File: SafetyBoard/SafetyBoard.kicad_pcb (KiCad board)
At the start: 4 copper layers, 154 x 93 mm, 170 parts, among them J1 Estop, J10 TSSI, J11 ACCU, J12 BBC, J13 614004135023, J14 footwell, J15 RTD B, J16 Brakelight, J17 SHOCK/WHEEL SNSR, J18 39306207, J19 AMP, J2 TS ON SW, J3 SDC OUT, J4 ACCU, J5 12v EXP, J6 PWR IN, J7 24v EXP, J8 5v EXP, J9 Current Sensor, K1 G6B-2214P-US DC12, K2 G6B-2214P-US DC12, K3 G6B-2214P-US DC12, Q1 IRLIZ44N NMOS, Q2 IRLIZ44N NMOS, Q3 IRLIZ44N NMOS, Q4 IRLIZ44N NMOS, Q5 PMOS IRF9540, Q6 PMOS IRF9540, Q7 PMOS IRF9540, SW1 SW_Push, SW2 SW_Push, SW3 SW_Push, U1 40106 Inverter, U2 4081 AND Gate, U3 LT1084-5.0, U4 LM393, U5 LM393, U6 CD4071BE OR Gate, U7 LM393, U8 LM555xN, U9 OKX-T/5-D12N-C

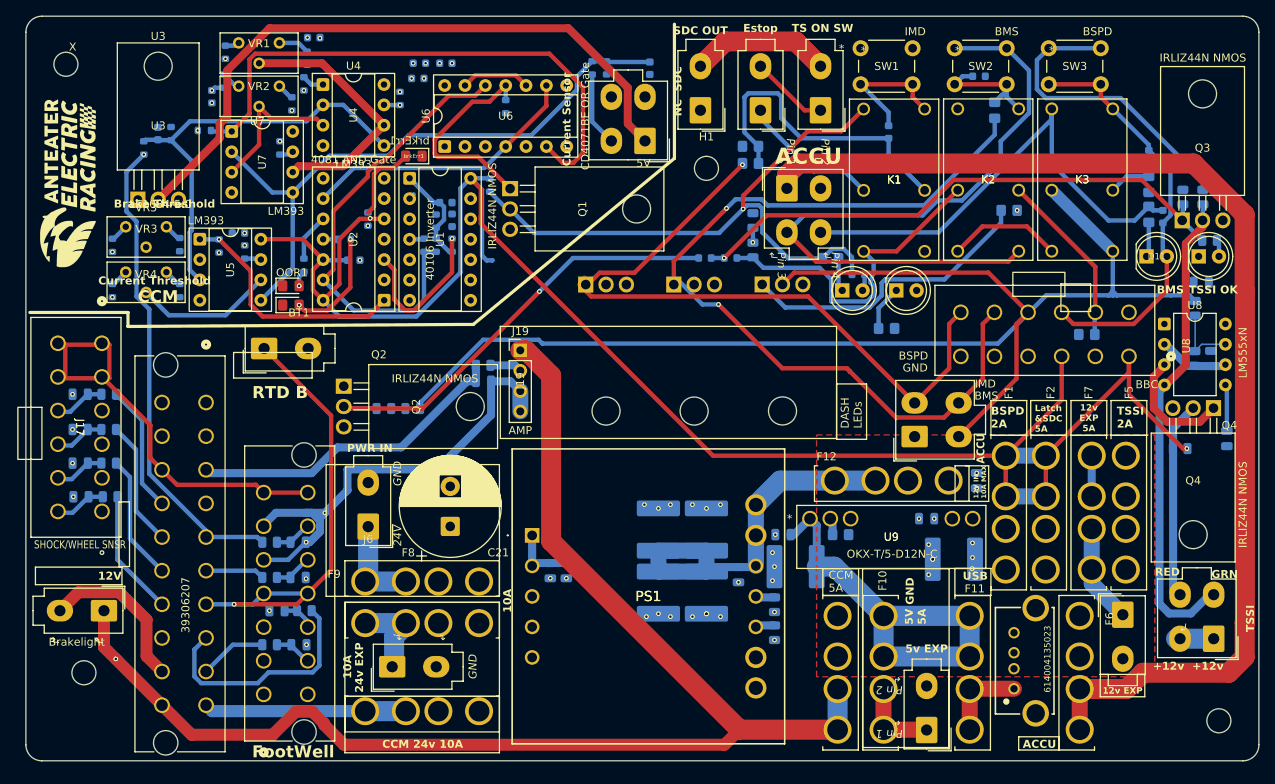
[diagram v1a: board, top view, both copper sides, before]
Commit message: Increased trace width
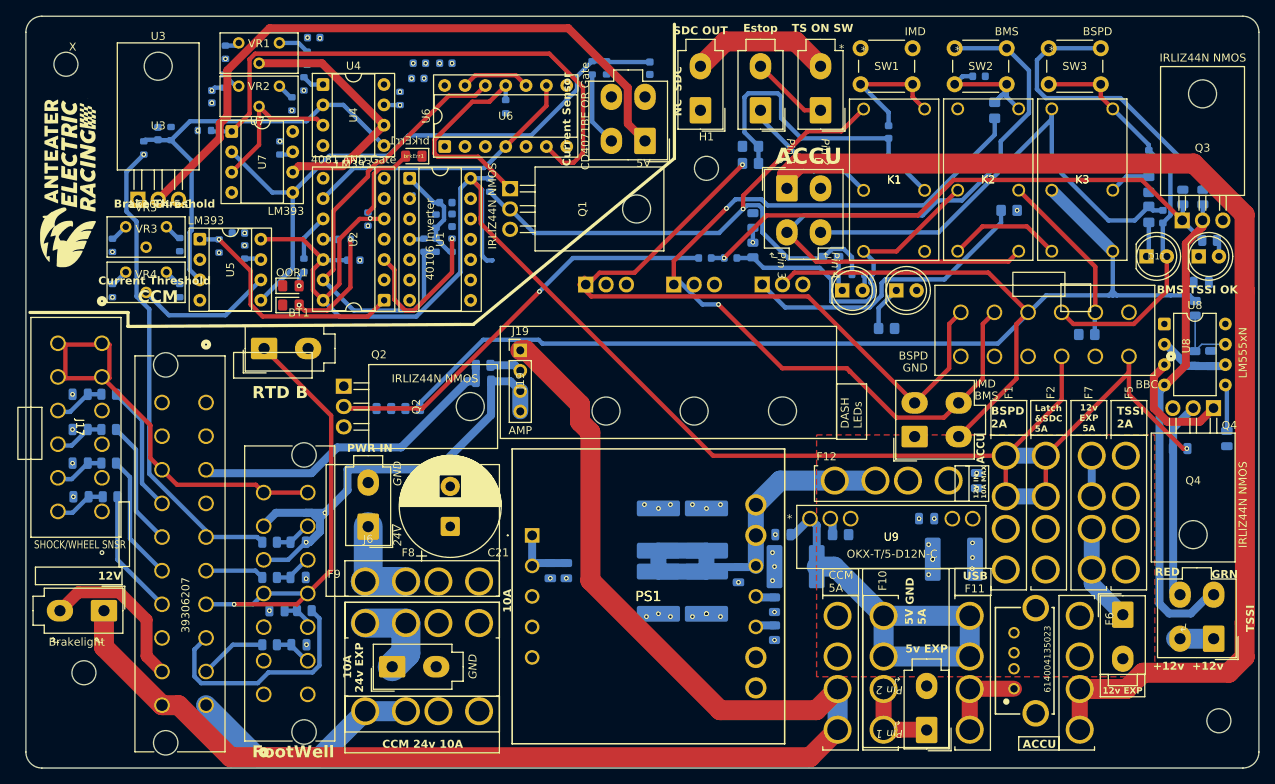
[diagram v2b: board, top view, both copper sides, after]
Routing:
- net /CCM Helper/12V: track 168.7 -> 179.8 mm, vias 1 -> 0
- net /CCM Helper/24V: track 25.3 -> 30.0 mm
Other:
- board size 154 x 93 mm -> 154 x 93.9 mm
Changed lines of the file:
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@@
 			)
 		)
-		(fp_text user "↲"
-			(at 3.048 1.27 90)
-			(unlocked yes)
-			(layer "F.SilkS")
-			(effects
-				(font
-					(size 1 1)
-					(thickness 0.1)
-					(italic yes)
-				)
-				(justify left bottom)
-			)
-		)
-		(fp_text user "↲"
-			(at 3.048 6.731 90)
-			(unlocked yes)
-			(layer "F.SilkS")
-			(effects
-				(font
-					(size 1 1)
-					(thickness 0.1)
-					(italic yes)
-				)
-				(justify left bottom)
-			)
-		)
 		(fp_text user "${REFERENCE}"
 			(at 0 -1.55 90)
@@
 	)
 	(gr_arc
-		(start 223 161)
-		(mid 222.414214 162.414214)
-		(end 221 163)
+		(start 223 161.9)
+		(mid 222.414214 163.314214)
+		(end 221 163.9)
 		(stroke
 			(width 0.05)
@@
 	(gr_line
 		(start 223 72)
-		(end 223 161)
+		(end 223 161.9)
 		(stroke
 			(width 0.05)
@@
 	)
 	(gr_arc
-		(start 71 163)
-		(mid 69.585786 162.414214)
-		(end 69 161)
+		(start 71 163.9)
+		(mid 69.585786 163.314214)
+		(end 69 161.9)
 		(stroke
 			(width 0.05)
@@
 	)
 	(gr_line
-		(start 221 163)
-		(end 71 163)
+		(start 221 163.9)
+		(end 71 163.9)
 		(stroke
 			(width 0.05)
@@
 	)
 	(gr_line
-		(start 69 161)
+		(start 69 161.9)
 		(end 69 72)
 		(stroke
@@
 		)
 	)
+	(dimension
+		(type orthogonal)
+		(layer "Dwgs.User")
+		(pts
+			(xy 71 70) (xy 71 163.9)
+		)
+		(height -10.9)
+		(orientation 1)
+		(format
+			(prefix "")
+			(suffix "")
+			(units 3)
+			(units_format 0)
+			(precision 4)
+			(suppress_zeroes yes)
+		)
+		(style
+			(thickness 0.1)
+			(arrow_length 1.27)
+			(text_position_mode 2)
+			(arrow_direction outward)
+			(extension_height 0.58642)
+			(extension_offset 0.5)
+			(keep_text_aligned yes)
+		)
+		(gr_text "93.9"
+			(at 58.6 117.1 90)
+			(layer "Dwgs.User")
+			(effects
+				(font
+					(size 1 1)
+					(thickness 0.15)
+				)
+			)
+		)
+	)
+	(dimension
+		(type orthogonal)
+		(layer "Dwgs.User")
+		(pts
+			(xy 223 71) (xy 69 71)
+		)
+		(height -3)
+		(orientation 0)
+		(format
+			(prefix "")
+			(suffix "")
+			(units 3)
+			(units_format 0)
+			(precision 4)
+			(suppress_zeroes yes)
+		)
+		(style
+			(thickness 0.1)
+			(arrow_length 1.27)
+			(text_position_mode 0)
+			(arrow_direction outward)
+			(extension_height 0.58642)
+			(extension_offset 0.5)
+			(keep_text_aligned yes)
+		)
+		(gr_text "154"
+			(at 146 66.85 0)
+			(layer "Dwgs.User")
+			(effects
+				(font
+					(size 1 1)
+					(thickness 0.15)
+				)
+			)
+		)
+	)
 	(via
 		(at 102.2245 81.7745)
@@
 	)
 	(segment
-		(start 106.265003 158.354112)
-		(end 106.265003 158.515003)
-		(width 1.5)
-		(layer "F.Cu")
-		(net 73)
-	)
-	(segment
-		(start 104.785892 156.875001)
-		(end 106.265003 158.354112)
-		(width 1.5)
+		(start 170.38 154.03)
+		(end 167.7365 156.6735)
+		(width 2.5)
 		(layer "F.Cu")
 		(net 73)
 	)
 	(segment
-		(start 102.694114 156.875001)
-		(end 104.785892 156.875001)
-		(width 1.5)
+		(start 86 156.049997)
+		(end 88.065015 156.049997)
+		(width 2.5)
 		(layer "F.Cu")
 		(net 73)
 	)
 	(segment
-		(start 99.819115 159.75)
-		(end 102.694114 156.875001)
-		(width 1.5)
+		(start 131.464106 111.7375)
+		(end 130.75 111.7375)
+		(width 2.5)
 		(layer "F.Cu")
 		(net 73)
 	)
 	(segment
-		(start 89.700003 159.75)
-		(end 99.819115 159.75)
-		(width 1.5)
+		(start 139.5 121.952808)
+		(end 138.209 120.661808)
+		(width 2.5)
 		(layer "F.Cu")
 		(net 73)
 	)
 	(segment
-		(start 86 156.049997)
-		(end 89.700003 159.75)
-		(width 1.5)
+		(start 138.209 118.482394)
+		(end 131.464106 111.7375)
+		(width 2.5)
 		(layer "F.Cu")
 		(net 73)
 	)
 	(segment
-		(start 170.38 159.11)
-		(end 158.133712 159.11)
+		(start 138.209 120.661808)
+		(end 138.209 118.482394)
 		(width 2.5)
 		(layer "F.Cu")
@@
 	)
 	(segment
-		(start 156.243712 161)
-		(end 158.133712 159.11)
-		(width 1.5)
+		(start 139.5 140.476288)
+		(end 139.5 121.952808)
+		(width 2.5)
 		(layer "F.Cu")
 		(net 73)
@@
 	(segment
 		(start 78.75 144.25)
-		(end 78.75 148.799998)
-		(width 1.5)
-		(layer "F.Cu")
-		(net 73)
-	)
-	(segment
-		(start 108.75 161)
-		(end 156.243712 161)
-		(width 1.5)
-		(layer "F.Cu")
-		(net 73)
-	)
-	(segment
-		(start 134.596 135.572288)
-		(end 134.596 114.869394)
+		(end 78.75 148.799997)
 		(width 2.5)
 		(layer "F.Cu")
@@
 	)
 	(segment
-		(start 134.596 114.869394)
-		(end 131.464106 111.7375)
+		(start 88.065015 156.049997)
+		(end 94.564018 162.549)
 		(width 2.5)
 		(layer "F.Cu")
@@
 	)
 	(segment
-		(start 106.265003 158.515003)
-		(end 108.75 161)
-		(width 1.5)
+		(start 166.941 162.549)
+		(end 170.38 159.11)
+		(width 2.5)
 		(layer "F.Cu")
 		(net 73)
 	)
 	(segment
-		(start 131.464106 111.7375)
-		(end 130.75 111.7375)
+		(start 155.697212 156.6735)
+		(end 139.5 140.476288)
 		(width 2.5)
 		(layer "F.Cu")
@@
 	)
 	(segment
-		(start 158.133712 159.11)
-		(end 134.596 135.572288)
+		(start 78.75 148.799997)
+		(end 86 156.049997)
 		(width 2.5)
 		(layer "F.Cu")
@@
 	)
 	(segment
-		(start 78.75 148.799998)
-		(end 80.225001 150.274999)
-		(width 1.5)
+		(start 167.7365 156.6735)
+		(end 155.697212 156.6735)
+		(width 2.5)
 		(layer "F.Cu")
 		(net 73)
 	)
 	(segment
-		(start 80.225001 150.274999)
-		(end 86 156.049997)
-		(width 1.5)
+		(start 94.564018 162.549)
+		(end 166.941 162.549)
+		(width 2.5)
 		(layer "F.Cu")
 		(net 73)
 	)
-	(via
-		(at 80.225001 150.274999)
-		(size 0.6)
-		(drill 0.3)
-		(layers "F.Cu" "B.Cu")
-		(net 73)
-	)
 	(segment
 		(start 170.38 159.11)
@@
 	)
 	(segment
-		(start 116.46 156.8)
-		(end 111.38 156.8)
+		(start 97.999002 162.549)
+		(end 91.499999 156.049997)
 		(width 2.5)
 		(layer "B.Cu")
@@
 	)
 	(segment
-		(start 91.499999 156.049997)
-		(end 92.250002 156.8)
-		(width 1.5)
+		(start 105.631 162.549)
+		(end 97.999002 162.549)
+		(width 2.5)
 		(layer "B.Cu")
 		(net 91)
 	)
 	(segment
-		(start 92.250002 156.8)
-		(end 111.38 156.8)
-		(width 1.5)
+		(start 111.38 156.8)
+		(end 105.631 162.549)
+		(width 2.5)
+		(layer "B.Cu")
+		(net 91)
+	)
+	(segment
+		(start 111.38 156.8)
+		(end 116.46 156.8)
+		(width 2.5)
 		(layer "B.Cu")
 		(net 91)
@@
 	)
 	(segment
-		(start 111.75 133.75)
-		(end 111.75 140.23)
-		(width 2.5)
+		(start 111.75 140.23)
+		(end 111.38 140.6)
+		(width 3.618)
 		(layer "B.Cu")
 		(net 101)
 	)
 	(segment
-		(start 111.75 140.23)
-		(end 111.38 140.6)
-		(width 2.5)
+		(start 111.75 133.75)
+		(end 111.75 140.23)
+		(width 3.618)
 		(layer "B.Cu")
 		(net 101)
@@
 		(start 116.46 140.6)
 		(end 111.38 140.6)
-		(width 2.5)
+		(width 3.618)
 		(layer "B.Cu")
 		(net 101)
@@
 	)
 	(segment
-		(start 116.46 146.04)
-		(end 116.46 145.8)
-		(width 2.5)
-		(layer "B.Cu")
-		(net 109)
-	)
-	(segment
-		(start 114.99 151.01)
-		(end 114.99 147.51)
-		(width 2.5)
-		(layer "B.Cu")
-		(net 109)
-	)
-	(segment
-		(start 114.75 151.25)
-		(end 114.99 151.01)
-		(width 2.5)
+		(start 116.46 145.8)
+		(end 116.46 149.54)
+		(width 3.618)
 		(layer "B.Cu")
 		(net 109)
 	)
 	(segment
-		(start 114.99 147.51)
-		(end 116.46 146.04)
-		(width 2.5)
+		(start 111.38 145.8)
+		(end 116.46 145.8)
+		(width 3.618)
 		(layer "B.Cu")
 		(net 109)
 	)
 	(segment
-		(start 116.46 145.8)
-		(end 111.38 145.8)
-		(width 2.5)
+		(start 116.46 149.54)
+		(end 114.75 151.25)
+		(width 3.618)
 		(layer "B.Cu")
 		(net 109)
@@
 		(min_thickness 0.25)
 		(filled_areas_thickness no)
-		(fill yes
+		(fill
 			(thermal_gap 0.5)
 			(thermal_bridge_width 0.5)
@@
 		(polygon
 			(pts
-				(xy 69 108.945768) (xy 93.386191 108.916933) (xy 93.3196 119.126) (xy 105.664 119.0752) (xy 106.1212 163)
-				(xy 69 163)
+				(xy 69 108.945768) (xy 93.386191 108.916933) (xy 93.3196 119.126) (xy 105.664 119.0752) (xy 106.128194 163.671996)
+				(xy 69 163.671996)
 			)
 		)
@@
 		(min_thickness 0.25)
 		(filled_areas_thickness no)
-		(fill yes
+		(fill
 			(thermal_gap 0.5)
 			(thermal_bridge_width 0.5)
@@
 		(polygon
 			(pts
-				(xy 223 71) (xy 69 71) (xy 69 163) (xy 223 163)
+				(xy 223 71) (xy 69 71) (xy 69 163.9) (xy 223 163.9)
 			)
 		)
@@
 		(min_thickness 0.25)
 		(filled_areas_thickness no)
-		(fill yes
+		(fill
 			(thermal_gap 0.5)
 			(thermal_bridge_width 0.5)
@@
 		(polygon
 			(pts
-				(xy 108.379175 126.743583) (xy 143.4084 126.6952) (xy 144.715885 163) (xy 108.75 163)
+				(xy 108.379175 126.743583) (xy 143.4084 126.6952) (xy 144.741095 163.7) (xy 108.757159 163.7)
 			)
 		)

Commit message: Minor updates
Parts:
- J4: value ACCU -> HVB
- moved R54 0.07 mm to (79.3, 121.5)
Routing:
- net +12V: track 408.6 -> 297.8 mm, vias 17 -> 16
- net /TSSI/GLV: track 4.20 -> 107.4 mm
- net Net-(J5-Pin_1): track 17.4 -> 10.6 mm
- net /12V: track 0.00 -> 4.24 mm
- net /LATCH/BSPDfault_LED: track 61.7 -> 58.4 mm
- net /LATCH/IMDfault_LED: track 56.6 -> 54.5 mm
- net /CCM Helper/CCMGND: track 60.2 -> 59.0 mm
- net Net-(Q4-G): track 14.9 -> 15.5 mm
- net Net-(brkErr1-A): vias 0 -> 1
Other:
- board text added: "HVB"
- board text removed: "ACCU"

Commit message: real final
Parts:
- removed BT1, OOR1: APTD2012LSYCK, LED_SMD:LED_0805_2012Metric_Pad1.15x1.40mm_HandSolder
- added BothThreshold1: APTD2012LSYCK, LED_SMD:LED_0805_2012Metric_Pad1.15x1.40mm_HandSolder, F.Cu at (102.3, 106.1)
- added OutOfRange1: APTD2012LSYCK, LED_SMD:LED_0805_2012Metric_Pad1.15x1.40mm_HandSolder, F.Cu at (102.2, 103.7)
- J1, J15, J16, J2, J3, J5, J6, J7, J8: footprint footprints:Molex_Mini-Fit_Jr_5566-02A_2x01_P4.20mm_Vertical -> 0footprints:Molex_Mini-Fit_Jr_5566-02A_2x01_P4.20mm_Vertical
- J10, J11, J9: footprint footprints:Molex_Mini-Fit_Jr_5566-04A_2x02_P4.20mm_Vertical -> 0footprints:Molex_Mini-Fit_Jr_5566-04A_2x02_P4.20mm_Vertical
- J4: value HVB -> ACCU; footprint footprints:Molex_Mini-Fit_Jr_5566-04A_2x02_P4.20mm_Vertical -> 0footprints:Molex_Mini-Fit_Jr_5566-04A_2x02_P4.20mm_Vertical
- brkErr1: moved to B.Cu
- moved H1 55.9 mm to (207.9, 74.1)
- moved R38 10.7 mm to (172.0, 110.7)
- moved D7 6.15 mm to (172.9, 108.4)
- moved C14 0.30 mm to (103.0, 148.2)
- moved C19 0.30 mm to (103.0, 139.8)
- moved J14 0.30 mm to (98.7, 154.4)
- moved SW3 0.25 mm to (196.5, 74.0)
- moved R55 0.22 mm to (79.3, 125.6)
- moved C15 0.21 mm to (100.3, 144.0)
- moved R46 0.21 mm to (103.7, 144.0)
- moved C18 0.21 mm to (103.0, 135.5)
- moved R45 0.21 mm to (99.4, 148.3)
- moved R47 0.21 mm to (99.4, 135.5)
- moved R48 0.21 mm to (99.4, 139.9)
- moved R56 0.12 mm to (79.5, 129.9)
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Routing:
- net +12V: track 297.8 -> 238.0 mm, vias 16 -> 30
- net /LATCH/BMSfault_LED: track 52.4 -> 88.9 mm, vias 0 -> 7
- net GND: track 0.00 -> 17.9 mm, vias 34 -> 59
- net /LATCH/BSPDfault_LED: track 58.4 -> 74.9 mm
- net Net-(J5-Pin_1): track 10.6 -> 25.3 mm
- net /LATCH/IMDfault_LED: track 54.5 -> 67.3 mm, vias 1 -> 6
- net /LATCH/bms_imd_latch_only: track 42.5 -> 31.1 mm, vias 0 -> 1
- net Net-(J6-Pin_1): track 12.7 -> 21.5 mm
- net /BSPD/PEDAL_OPEN: track 31.8 -> 39.3 mm, vias 0 -> 3
- net Net-(J7-Pin_1): track 11.2 -> 18.1 mm
- net /BSPD/BSPD_FAULT: track 77.6 -> 83.9 mm
- net /CCM Helper/CCM fdbk: track 81.9 -> 87.4 mm, vias 1 -> 2
- net /12V: track 4.24 -> 0.00 mm
- net Net-(D2-K): track 70.5 -> 74.5 mm
- net Net-(D6-K): track 4.80 -> 8.55 mm, vias 0 -> 1
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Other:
- board text added: "OC"
- board text added: "SC"
- board text added: "Safety Board By: Gabriel Schoene, Lucas Li, Avadi Seneviratne"
- board text added: "cursns"
- board text removed: "CCM"
- board text removed: "Safety Board By: Gabriel Schoene"

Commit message: double checking its all pushed
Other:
- board text added: "there better be a dummy plug in SDC con"
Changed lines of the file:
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@@
 		)
 		(property "Value" "Brakelight"
-			(at 0 9.95 270)
+			(at 9.45 7.35 270)
 			(layer "F.SilkS")
 			(effects
@@
 			(layer "F.Fab")
 		)
-		(fp_text user "↲"
-			(at 3.048 1.27 270)
-			(unlocked yes)
-			(layer "F.SilkS")
-			(effects
-				(font
-					(size 1 1)
-					(thickness 0.1)
-					(italic yes)
-				)
-				(justify left bottom)
-			)
-		)
-		(fp_text user "↲"
-			(at 3.048 6.731 270)
-			(unlocked yes)
-			(layer "F.SilkS")
-			(effects
-				(font
-					(size 1 1)
-					(thickness 0.1)
-					(italic yes)
-				)
-				(justify left bottom)
-			)
-		)
-		(fp_text user "Pin 1"
-			(at 2.921 0.127 270)
-			(unlocked yes)
-			(layer "F.SilkS")
-			(effects
-				(font
-					(size 1 1)
-					(thickness 0.125)
-					(italic yes)
-				)
-				(justify left bottom)
-			)
-		)
-		(fp_text user "Pin 2"
-			(at 2.921 5.588 270)
-			(unlocked yes)
-			(layer "F.SilkS")
-			(effects
-				(font
-					(size 1 1)
-					(thickness 0.125)
-					(italic yes)
-				)
-				(justify left bottom)
-			)
-		)
 		(fp_text user "${REFERENCE}"
 			(at 0 -1.55 270)
@@
 		)
 	)
+	(gr_text "GND"
+		(at 71.9 140.7 0)
+		(layer "F.SilkS")
+		(effects
+			(font
+				(size 1 1)
+				(thickness 0.1)
+			)
+			(justify left bottom)
+		)
+	)
 	(gr_text "IMD"
 		(at 178.75 72.5 0)
@@
 		)
 	)
+	(gr_text "there better \nbe a dummy plug \nin SDC con"
+		(at 151.3 85.8 270)
+		(layer "F.SilkS")
+		(effects
+			(font
+				(size 1 1)
+				(thickness 0.1)
+			)
+			(justify left bottom)
+		)
+	)
 	(gr_text "BMS"
 		(at 210.235 104.75 0)
@@
 		)
 	)
+	(gr_text "IMD"
+		(at 177.9 109 0)
+		(layer "F.SilkS")
+		(effects
+			(font
+				(size 1 1)
+				(thickness 0.1)
+			)
+			(justify left bottom)
+		)
+	)
 	(gr_text "+12v  +12v"
 		(at 209.75 151.75 0)
@@
 		(layer "F.SilkS")
 		(effects
+			(font
+				(size 1 1)
+				(thickness 0.1)
+			)
+			(justify left bottom)
+		)
+	)
+	(gr_text "BSPD"
+		(at 170.25 108.7375 0)
+		(layer "F.SilkS")
+		(effects

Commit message: 3d component changes
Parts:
- F1, F10, F11, F12, F2, F3, F4, F5, F6, F7, F8, F9: footprint 0footprints:FUSE_3522-2 -> footprints:FUSE_3522-2
- J1, J15, J16, J2, J3, J5, J6, J7, J8: footprint 0footprints:Molex_Mini-Fit_Jr_5566-02A_2x01_P4.20mm_Vertical -> footprints:Molex_Mini-Fit_Jr_5566-02A_2x01_P4.20mm_Vertical
- J10, J11, J4, J9: footprint 0footprints:Molex_Mini-Fit_Jr_5566-04A_2x02_P4.20mm_Vertical -> footprints:Molex_Mini-Fit_Jr_5566-04A_2x02_P4.20mm_Vertical
